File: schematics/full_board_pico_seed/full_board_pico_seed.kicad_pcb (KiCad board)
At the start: 4 copper layers, 128.3 x 74.9 mm, 148 parts, among them J1 XLR3, J10 Conn_02x20_Odd_Even, J12 Conn_01x01_Female, J13 Conn_01x01_Female, J2 Conn_01x02_Male, J3 Aux In, J4 Conn_01x02_Pin, J5 Conn_02x03_Odd_Even, J6 Conn_01x03_Female, J7 XLR3, J8 XLR3, J9 Conn_01x03, P0 25k, P1 25k, P2 25k, SW1 Stompbutton 1, SW2 Stompbutton 2, SW3 Stompbutton 3, SW4 Enter, SW5 Exit, U1 TL074, U10 LM4881M/NOPB, U11 CS4270-CZZ, U12 128X64 OLED Display, U14 AP63205WU, U3 LM1117DT-5.0, U4 NE5534, U5 ATmega88A-A, U6 24LC128, U7 MC78M05_TO252, U9 TL074, X1 SG-5032CAN

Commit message: minor corrections
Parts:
- moved R46 5.75 mm to (140.5, 92.2), turned to 180 degrees
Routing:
- net GND: track 244.5 -> 238.9 mm
- net Net-(C29-Pad1): track 15.2 -> 9.97 mm
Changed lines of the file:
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@@
   )
   (footprint "Resistor_SMD:R_0603_1608Metric_Pad0.98x0.95mm_HandSolder" (layer "F.Cu")
-    (at 143.415 97.137025 90)
+    (at 140.462 92.202 180)
     (descr "Resistor SMD 0603 (1608 Metric), square (rectangular) end terminal, IPC_7351 nominal with elongated pad for handsoldering. (Body size source: IPC-SM-782 page 72, https://www.pcb-3d.com/wordpress/wp-content/uploads/ipc-sm-782a_amendment_1_and_2.pdf), generated with kicad-footprint-generator")
     (tags "resistor handsolder")
@@
     (property "ki_keywords" "R res resistor")
     (attr smd)
-    (fp_text reference "R46" (at 0 -1.43 90) (layer "F.SilkS")
+    (fp_text reference "R46" (at -1.524 -1.524 180) (layer "F.SilkS")
         (effects (font (size 1 1) (thickness 0.15)))
     )
-    (fp_text value "10k" (at 0 1.43 90) (layer "F.Fab")
+    (fp_text value "10k" (at 0 1.43) (layer "F.Fab")
         (effects (font (size 1 1) (thickness 0.15)))
     )
-    (fp_text user "${REFERENCE}" (at 0 0 90) (layer "F.Fab")
+    (fp_text user "${REFERENCE}" (at 0 0) (layer "F.Fab")
         (effects (font (size 0.4 0.4) (thickness 0.06)))
     )
@@
     (fp_line (start 0.8 0.4125) (end -0.8 0.4125)
       (stroke (width 0.1) (type solid)) (layer "F.Fab"))
-    (pad "1" smd roundrect (at -0.9125 0 90) (size 0.975 0.95) (layers "F.Cu" "F.Paste" "F.Mask") (roundrect_rratio 0.25)
+    (pad "1" smd roundrect (at -0.9125 0 180) (size 0.975 0.95) (layers "F.Cu" "F.Paste" "F.Mask") (roundrect_rratio 0.25)
       (net 2 "GND") (pintype "passive"))
-    (pad "2" smd roundrect (at 0.9125 0 90) (size 0.975 0.95) (layers "F.Cu" "F.Paste" "F.Mask") (roundrect_rratio 0.25)
+    (pad "2" smd roundrect (at 0.9125 0 180) (size 0.975 0.95) (layers "F.Cu" "F.Paste" "F.Mask") (roundrect_rratio 0.25)
       (net 85 "Net-(C29-Pad1)") (pintype "passive"))
     (model "${KICAD6_3DMODEL_DIR}/Resistor_SMD.3dshapes/R_0603_1608Metric.wrl"
@@
   (segment (start 87.8175 131.9475) (end 89.22 133.35) (width 0.35) (layer "F.Cu") (net 2))
   (segment (start 123.155 112.601525) (end 125.007 110.749525) (width 0.35) (layer "F.Cu") (net 2))
-  (segment (start 144.265 89.567525) (end 143.52 88.822525) (width 0.35) (layer "F.Cu") (net 2))
   (segment (start 187.865 82.930025) (end 188.8525 83.917525) (width 0.35) (layer "F.Cu") (net 2))
   (segment (start 104.54 112.540525) (end 105.315 111.765525) (width 0.35) (layer "F.Cu") (net 2))
@@
   (segment (start 147.1025 71.115313) (end 147.454712 71.467525) (width 0.35) (layer "F.Cu") (net 2))
   (segment (start 95.598 115.951) (end 95.598 119.761) (width 0.35) (layer "F.Cu") (net 2))
+  (segment (start 141.3745 90.968025) (end 143.52 88.822525) (width 0.35) (layer "F.Cu") (net 2))
   (segment (start 135.3085 91.445525) (end 135.3085 90.408025) (width 0.35) (layer "F.Cu") (net 2))
   (segment (start 169.545 98.425) (end 169.418 98.298) (width 0.35) (layer "F.Cu") (net 2))
@@
   (segment (start 149.3345 85.222525) (end 149.235 85.123025) (width 0.35) (layer "F.Cu") (net 2))
   (segment (start 196.085 83.917525) (end 198.025 85.857525) (width 0.35) (layer "F.Cu") (net 2))
-  (segment (start 144.265 97.199525) (end 144.265 89.567525) (width 0.35) (layer "F.Cu") (net 2))
+  (segment (start 141.3745 92.202) (end 141.3745 90.968025) (width 0.35) (layer "F.Cu") (net 2))
   (segment (start 123.9575 97.686427) (end 123.598701 98.045226) (width 0.35) (layer "F.Cu") (net 2))
   (segment (start 116.045 89.375025) (end 111.919 89.375025) (width 0.35) (layer "F.Cu") (net 2))
-  (segment (start 143.415 98.049525) (end 144.265 97.199525) (width 0.35) (layer "F.Cu") (net 2))
   (segment (start 108.363 103.465525) (end 106.667 103.465525) (width 0.35) (layer "F.Cu") (net 2))
   (segment (start 98.095 111.022525) (end 99.795 111.022525) (width 0.35) (layer "F.Cu") (net 2))
@@
   (segment (start 104.045 66.172525) (end 107.055 69.182525) (width 0.25) (layer "F.Cu") (net 84))
   (segment (start 107.055 69.182525) (end 108.855 69.182525) (width 0.25) (layer "F.Cu") (net 84))
-  (segment (start 143.114 96.525525) (end 143.415 96.224525) (width 0.25) (layer "F.Cu") (net 85))
-  (segment (start 139.351 91.445525) (end 141.891 93.985525) (width 0.25) (layer "F.Cu") (net 85))
-  (segment (start 141.891 94.700525) (end 143.415 96.224525) (width 0.25) (layer "F.Cu") (net 85))
-  (segment (start 139.351 86.666525) (end 139.351 91.445525) (width 0.25) (layer "F.Cu") (net 85))
-  (segment (start 139.627 96.525525) (end 143.114 96.525525) (width 0.25) (layer "F.Cu") (net 85))
-  (segment (start 141.891 93.985525) (end 141.891 94.700525) (width 0.25) (layer "F.Cu") (net 85))
+  (segment (start 139.627 96.525525) (end 139.627 92.2795) (width 0.25) (layer "F.Cu") (net 85))
+  (segment (start 139.351 86.666525) (end 139.351 92.0035) (width 0.25) (layer "F.Cu") (net 85))
+  (segment (start 139.627 92.2795) (end 139.5495 92.202) (width 0.25) (layer "F.Cu") (net 85))
+  (segment (start 139.351 92.0035) (end 139.5495 92.202) (width 0.25) (layer "F.Cu") (net 85))
   (segment (start 118.272406 100.081525) (end 126.651 100.081525) (width 0.25) (layer "F.Cu") (net 86))
   (segment (start 115.494188 99.065525) (end 117.256406 99.065525) (width 0.25) (layer "F.Cu") (net 86))

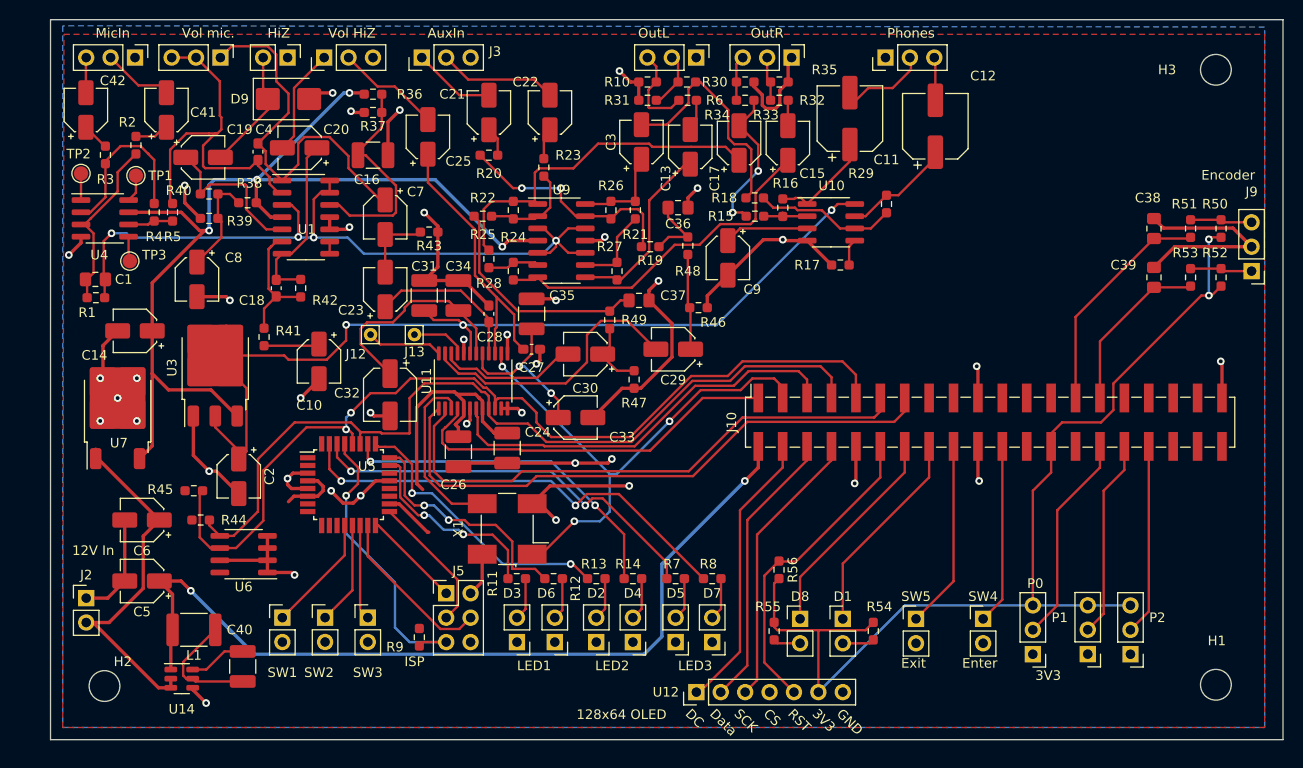
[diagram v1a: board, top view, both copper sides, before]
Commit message: added adapter board for raspberryy pi pico
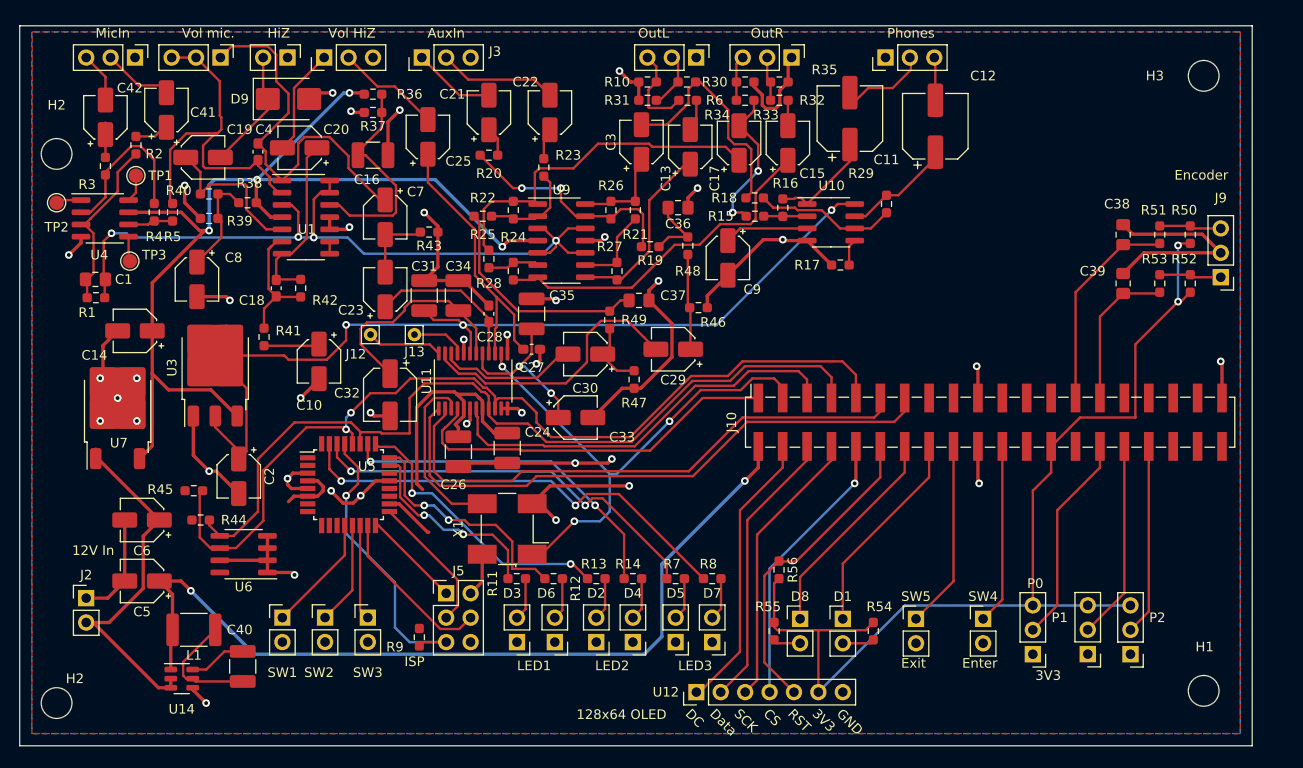
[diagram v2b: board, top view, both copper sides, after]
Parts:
- added H2: MountingHole, MountingHole:MountingHole_3.2mm_M3, F.Cu at (73.7, 76.2)
- moved H2 5.29 mm to (73.7, 133.3)
- moved TP2 3.97 mm to (73.7, 81.3)
- moved C38 3.27 mm to (184.7, 84.6)
- moved C39 3.27 mm to (184.7, 89.7)
- moved R51 3.27 mm to (188.5, 84.6)
- moved R53 3.27 mm to (188.5, 89.7)
- moved J9 3.27 mm to (194.8, 89.0)
- moved R50 3.27 mm to (191.6, 84.6)
- moved R52 3.27 mm to (191.6, 89.7)
- moved C42 2.17 mm to (78.7, 72.4)
- moved H1 1.42 mm to (193.0, 132.1)
- moved H3 1.42 mm to (193.0, 68.1)
- moved R3 1.17 mm to (78.7, 77.5)
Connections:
- J10 pad 10: GND -> Net-(J10-Pin_10)
- U12 pad 4: GND -> Net-(J10-Pin_10)
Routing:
- net Net-(J10-Pin_10): track 0.00 -> 29.3 mm, vias 0 -> 1
- net GND: track 238.9 -> 235.3 mm, vias 40 -> 39
- net Net-(C42-Pad1): track 2.85 -> 4.84 mm
- net Net-(J10-Pin_27): track 23.8 -> 21.9 mm
- net Net-(J10-Pin_29): track 17.7 -> 15.7 mm
- net Net-(C42-Pad2): track 3.67 -> 5.29 mm
- net Net-(U4--): track 17.8 -> 17.1 mm

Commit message: pcd: changed innductor footprint
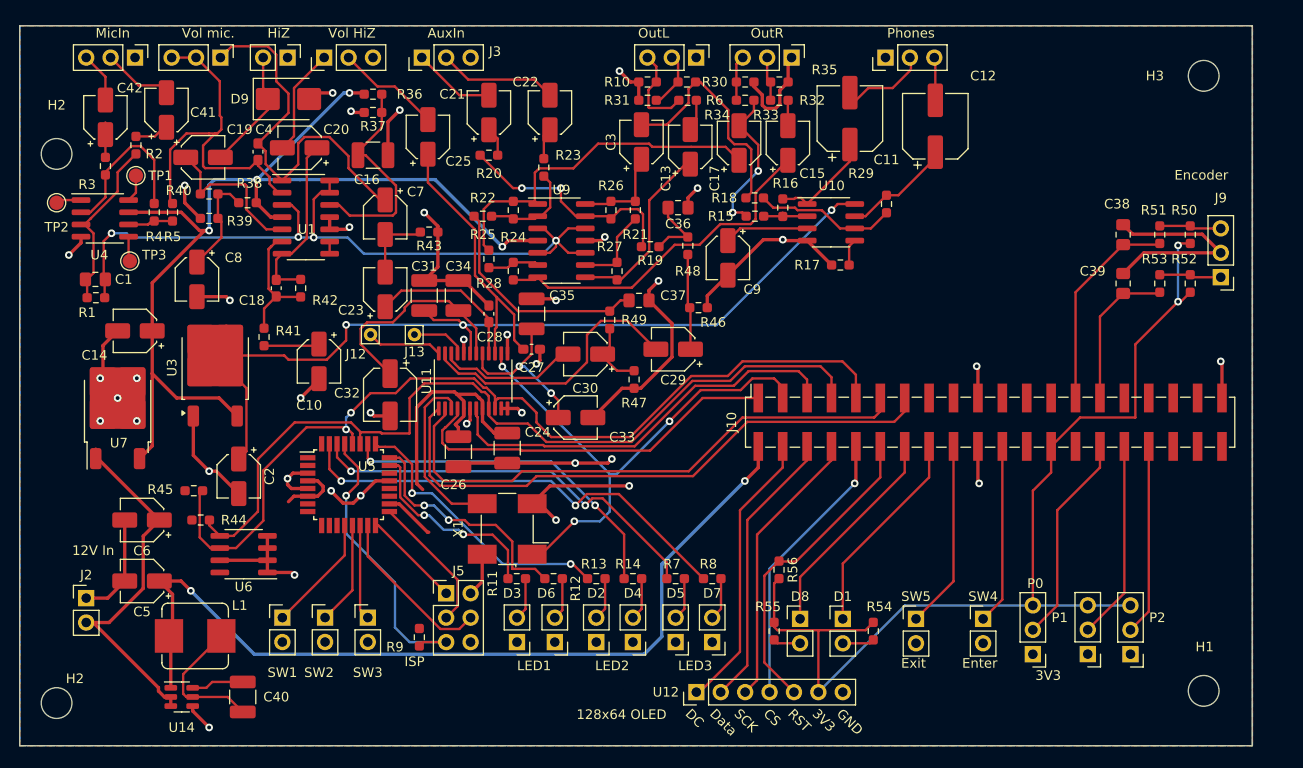
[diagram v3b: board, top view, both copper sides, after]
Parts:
- L1: footprint Inductor_SMD:L_1812_4532Metric_Pad1.30x3.40mm_HandSolder -> Inductor_SMD:L_Bourns_SRP7028A_7.3x6.6mm
- U3: footprint Package_TO_SOT_SMD:TO-252-3_TabPin2 -> Package_TO_SOT_SMD:TO-252-2
- moved C40 3.18 mm to (93.0, 132.7)
- moved U14 1.91 mm to (86.7, 132.7)
- moved L1 0.65 mm to (88.1, 126.4)
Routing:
- net 5V: track 99.2 -> 94.6 mm
- net Net-(U14-SW): track 12.6 -> 14.7 mm
- net 5V_DIG: track 90.0 -> 91.9 mm
- net GND: track 235.3 -> 236.0 mm
- net Vin: track 38.0 -> 38.6 mm
- net Net-(U14-BST): track 5.99 -> 5.47 mm

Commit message: more work on full schematic: added test points
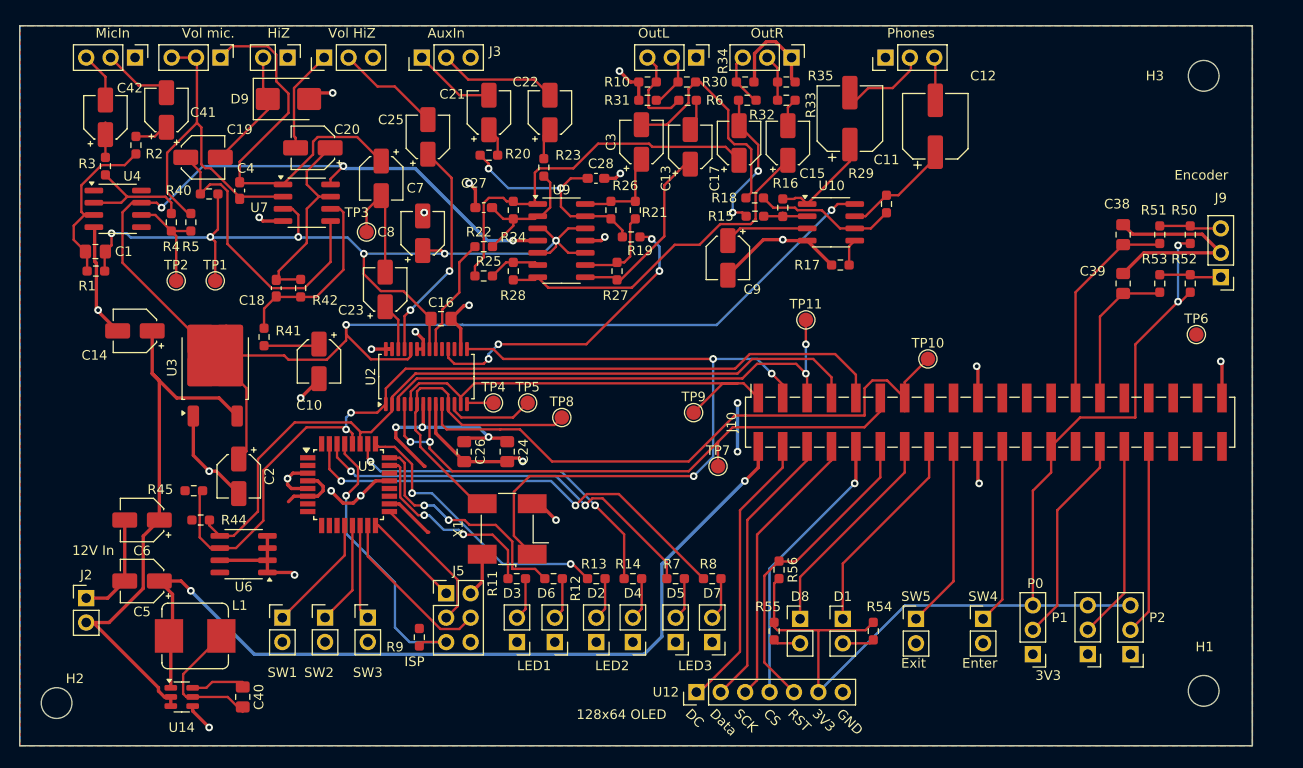
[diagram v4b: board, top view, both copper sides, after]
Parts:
- removed C29, C30: 3.3uF, Capacitor_SMD:CP_Elec_4x4.5
- removed C31, C34, C35: 0.1uF, Capacitor_SMD:C_1210_3225Metric_Pad1.33x2.70mm_HandSolder
- removed C32: 47uF, Capacitor_SMD:CP_Elec_5x5.4
- removed C33: 10uF, Capacitor_SMD:CP_Elec_4x4.5
- removed C36, C37: 3.3nF, Capacitor_SMD:C_0805_2012Metric_Pad1.18x1.45mm_HandSolder
- removed the H2 at (73.7, 76.2)
- removed J12, J13: Conn_01x01_Female, Connector_Pin:Pin_D0.7mm_L6.5mm_W1.8mm_FlatFork
- removed R36, R37, R38, R39: 12k, Resistor_SMD:R_0603_1608Metric_Pad0.98x0.95mm_HandSolder
- removed R43: 47k, Resistor_SMD:R_0603_1608Metric_Pad0.98x0.95mm_HandSolder
- removed R46, R47: 10k, Resistor_SMD:R_0603_1608Metric_Pad0.98x0.95mm_HandSolder
- removed R48, R49: 470, Resistor_SMD:R_0603_1608Metric_Pad0.98x0.95mm_HandSolder
- removed U1: TL074, Package_SO:SOIC-14_3.9x8.7mm_P1.27mm
- removed U11: CS4270-CZZ, Package_SO:TSSOP-24_4.4x7.8mm_P0.65mm
- added TP10: TestPoint, TestPoint:TestPoint_Pad_D1.5mm, F.Cu at (164.3, 97.5)
- added TP11: TestPoint, TestPoint:TestPoint_Pad_D1.5mm, F.Cu at (151.6, 93.5)
- added TP4: TestPoint, TestPoint:TestPoint_Pad_D1.5mm, F.Cu at (119.1, 102.1)
- added TP5: TestPoint, TestPoint:TestPoint_Pad_D1.5mm, F.Cu at (122.7, 102.1)
- added TP6: TestPoint, TestPoint:TestPoint_Pad_D1.5mm, F.Cu at (192.3, 95.0)
- added TP7: TestPoint, TestPoint:TestPoint_Pad_D1.5mm, F.Cu at (142.5, 108.7)
- added TP8: TestPoint, TestPoint:TestPoint_Pad_D1.5mm, F.Cu at (126.2, 103.6)
- added TP9: TestPoint, TestPoint:TestPoint_Pad_D1.5mm, F.Cu at (140.0, 103.1)
- added U2: PCM3060PWR, Package_SO:TSSOP-28_4.4x9.7mm_P0.65mm, F.Cu at (112.1, 99.4)
- C14: value 22uF -> 10uF
- C16: value 0.1uF -> 0.1u; footprint Capacitor_SMD:C_1210_3225Metric_Pad1.33x2.70mm_HandSolder -> Capacitor_SMD:C_0805_2012Metric_Pad1.18x1.45mm_HandSolder
- C2: value 1uF -> 56uF
- C24, C26, C40: footprint Capacitor_SMD:C_1210_3225Metric_Pad1.33x2.70mm_HandSolder -> Capacitor_SMD:C_0805_2012Metric_Pad1.18x1.45mm_HandSolder
- C27, C28: value 220pF -> 330p
- C8: value 1uF -> 10u
- U4: value NE5534 -> OPA134
- U7: value MC78M05_TO252 -> OPA2342; footprint Package_TO_SOT_SMD:TO-252-2 -> Package_SO:SOIC-8_3.9x4.9mm_P1.27mm
- U9: value TL074 -> OPA4342
- moved U7 29.2 mm to (99.7, 81.3), turned to 0 degrees
- moved TP3 24.8 mm to (105.9, 84.3)
- moved C8 24.0 mm to (111.8, 84.5), turned to 90 degrees
- moved C16 18.4 mm to (113.7, 93.3)
- moved C28 18.0 mm to (129.8, 78.7), turned to 180 degrees
- moved C27 15.6 mm to (118.1, 81.8), turned to 0 degrees
- moved TP2 14.9 mm to (86.1, 89.4)
- moved TP1 13.7 mm to (90.2, 89.4)
- moved C4 4.46 mm to (92.7, 80.0)
- moved R33 4.29 mm to (149.6, 70.6)
- moved C7 4.07 mm to (107.4, 78.7)
- moved R32 3.34 mm to (145.5, 70.6)
- moved R22 3.17 mm to (118.1, 85.9)
- moved C1 2.90 mm to (77.7, 86.4)
- moved R1 2.77 mm to (77.7, 88.4)
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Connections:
- C1 pad 1: VGND -> /Analog Preamp/VCom
- C14 pad 1: +9V -> Vin
- C16 pad 1: Net-(U1D-+) -> /Analog Preamp/VCom
- C18 pad 1: Net-(U1B--) -> Net-(U7B--)
- C19 pad 1: Net-(U1B-+) -> Net-(U7B-+)
- C23 pad 1: Net-(U11-AINB) -> Net-(U2-VINR)
- C25 pad 1: Net-(U11-AINA) -> Net-(U2-VINL)
- C27 pad 2: Net-(U11-AINA) -> Net-(U9A--)
- C28 pad 2: Net-(U11-AINB) -> Net-(U9D--)
- C4 pad 1: Net-(U1A--) -> Net-(U7A--)
- C8 pad 1: Net-(C8-Pad1) -> /Analog Preamp/VCom
- J10 pad 26: Net-(J10-Pin_26) -> 3V3
- P0 pad 3: Net-(J10-Pin_26) -> 3V3
- P1 pad 3: Net-(J10-Pin_26) -> 3V3
- P2 pad 3: Net-(J10-Pin_26) -> 3V3
- R1 pad 1: VGND -> /Analog Preamp/VCom
- R19 pad 1: /Analog Preamp/DacR -> /Analog Preamp/DacR+
- R22 pad 1: /Analog Preamp/DacL -> /Analog Preamp/DacL+
- R32 pad 1: Net-(J8-Pad2) -> /Analog Preamp/Left Analog Out
- R32 pad 2: Net-(C15-Pad2) -> Net-(J8-Pad3)
- R33 pad 1: /Analog Preamp/Left Analog Out -> Net-(C15-Pad2)
- R33 pad 2: Net-(J8-Pad3) -> Net-(J8-Pad2)
- R35 pad 1: Net-(J8-Pad2) -> GND
- R35 pad 2: GND -> Net-(J8-Pad2)
- R40 pad 1: Net-(C8-Pad1) -> /Analog Preamp/VCom
- R40 pad 2: Net-(U1B-+) -> Net-(U7B-+)
- R41 pad 1: Net-(U1B--) -> Net-(U7B--)
- R42 pad 1: Net-(U1B--) -> Net-(U7B--)
- R5 pad 1: Net-(U1A--) -> Net-(U7A--)
- R50 pad 1: Net-(J10-Pin_26) -> 3V3
- R52 pad 1: Net-(J10-Pin_26) -> 3V3
- R54 pad 2: Net-(J10-Pin_26) -> 3V3
- R55 pad 2: Net-(J10-Pin_26) -> 3V3
- R56 pad 2: Net-(J10-Pin_26) -> 3V3
- RV1 pad 2: Net-(U1A--) -> Net-(U7A--)
- RV1 pad 3: Net-(U1A--) -> Net-(U7A--)
- TP1 pad 1: Net-(U4-C/B) -> /Analog Preamp/VCom
- TP2 pad 1: Net-(U4-BAL) -> Net-(R4-Pad2)
- TP3 pad 1: Net-(U4-COMP) -> /Analog Preamp/Mic
- U12 pad 6: Net-(J10-Pin_26) -> 3V3
- U3 pad 3: +9V -> Vin
- U4 pad 1: Net-(U4-BAL) -> unconnected-(U4-BAL-Pad1)
- U4 pad 5: Net-(U4-COMP) -> unconnected-(U4-COMP-Pad5)
- U4 pad 7: +9V -> 5V
- U4 pad 8: Net-(U4-C/B) -> unconnected-(U4-C/B-Pad8)
- U7 pad 1: Vin -> Net-(C4-Pad2)
- U7 pad 2: GND -> Net-(U7A--)
- U7 pad 3: +9V -> /Analog Preamp/VCom
- U9 pad 10: VGND -> /Analog Preamp/VCom
- U9 pad 12: VGND -> /Analog Preamp/VCom
- U9 pad 3: VGND -> /Analog Preamp/VCom
- U9 pad 4: +9V -> 5V
- U9 pad 5: VGND -> /Analog Preamp/VCom
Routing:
- net +9V: track 111.1 -> 0.00 mm, vias 4 -> 0
- net 3V3: track 43.3 -> 153.8 mm, vias 0 -> 7
- net Net-(J10-Pin_26): track 109.8 -> 0.00 mm, vias 2 -> 0
- net /Analog Preamp/VCom: track 0.00 -> 95.6 mm, vias 0 -> 6
- net VGND: track 79.0 -> 0.00 mm, vias 4 -> 0
- net 5V: track 94.6 -> 166.4 mm, vias 3 -> 5
- net GND: track 236.0 -> 167.5 mm, vias 39 -> 24
- net Net-(U1A--): track 37.8 -> 0.00 mm
- net Net-(U7A--): track 0.00 -> 36.0 mm
- net /Analog Preamp/DacR+: track 0.00 -> 32.4 mm, vias 0 -> 4
- net Net-(U7B-+): track 0.00 -> 31.5 mm
- net Net-(U11-AINA): track 30.3 -> 0.00 mm
- net Net-(U11-AOUTB): track 29.2 -> 0.00 mm
- net /Analog Preamp/DacL: track 23.8 -> 0.00 mm
- net Net-(U1D-+): track 23.4 -> 0.00 mm
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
